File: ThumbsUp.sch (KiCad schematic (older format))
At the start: 159 parts, among them J17 Raiser_Female, J18 Raiser_Male, J19 52559-1233, J32 Battery, SW1 SW_Push, SW2 SW_DIP_x01, U1 ProMicro

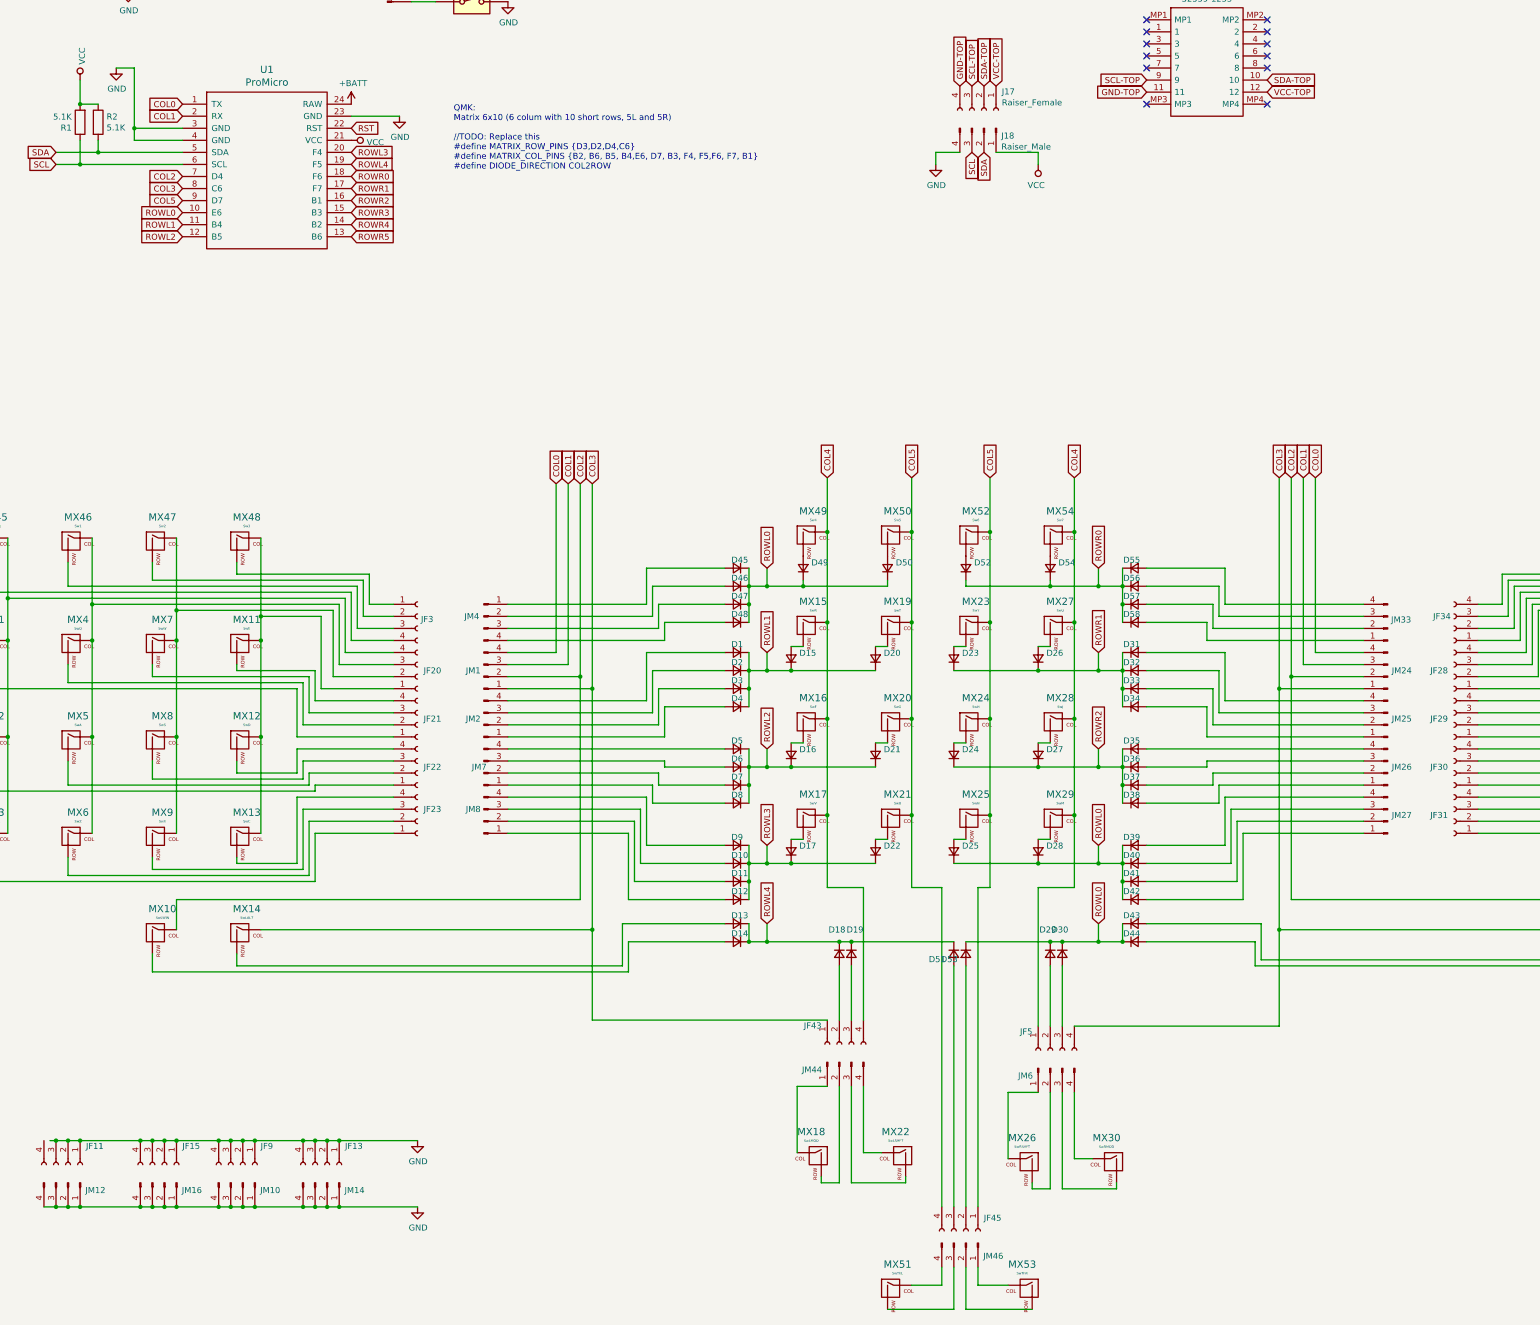
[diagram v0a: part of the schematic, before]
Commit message: Layed out switches and cross-plate connectors
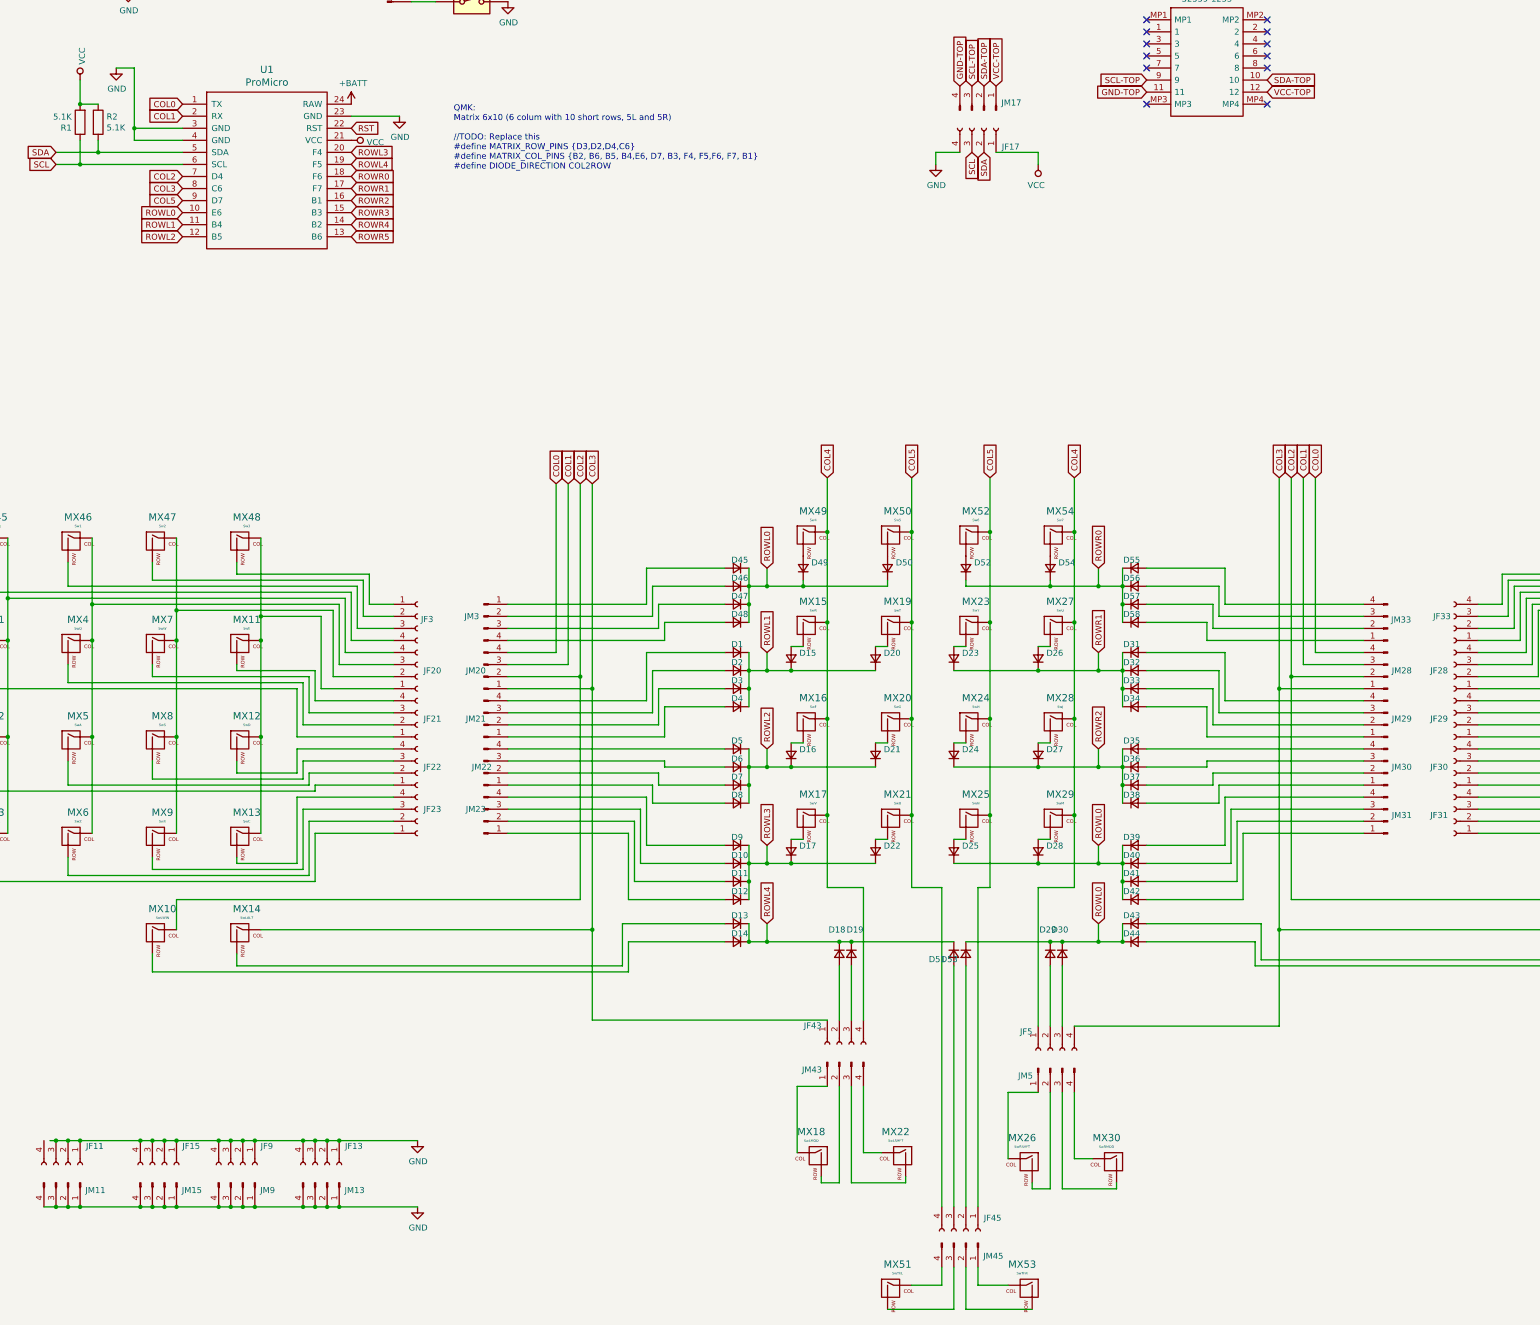
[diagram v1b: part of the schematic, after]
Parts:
- MX1, MX10, MX11, MX12, MX13, MX14, MX15, MX16, MX17, MX18, MX19, MX2, MX20, MX21, MX22, MX23, MX24, MX25, MX26, MX27, MX28, MX29, MX3, MX30, MX31, MX32, MX33, MX34, MX35, MX36, MX37, MX38, MX39, MX4, MX40, MX41, MX42, MX43, MX44, MX45, MX46, MX47, MX48, MX49, MX5, MX50, MX51, MX52, MX53, MX54, MX55, MX56, MX57, MX58, MX6, MX7, MX8, MX9: footprint keyswitches:Kailh_socket_PG1350_optional -> MX_Alps_Hybrid:MX-1U-NoLED_HotSwap
- renumbered J17 to JF17, JF34 to JF33, JM12 to JM11, JM14 to JM13, JM16 to JM15, J18 to JM17, JM1 to JM20, JM2 to JM21, JM7 to JM22, JM8 to JM23, JM24 to JM28, JM25 to JM29, JM4 to JM3, JM26 to JM30, JM27 to JM31, JM44 to JM43, JM46 to JM45, JM6 to JM5, JM10 to JM9
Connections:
- net GND: now also JF17.4 (Pin_4); no longer JM17.4 (Pin_4)
- net GND-TOP: now also JM17.4 (Pin_4); no longer JF17.4 (Pin_4)
- net SCL: now also JF17.3 (Pin_3); no longer JM17.3 (Pin_3)
- net SCL-TOP: now also JM17.3 (Pin_3); no longer JF17.3 (Pin_3)
- net SDA: now also JF17.2 (Pin_2); no longer JM17.2 (Pin_2)
- net SDA-TOP: now also JM17.2 (Pin_2); no longer JF17.2 (Pin_2)
- net VCC: now also JF17.1 (Pin_1); no longer JM17.1 (Pin_1)
- net VCC-TOP: now also JM17.1 (Pin_1); no longer JF17.1 (Pin_1)
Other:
- moved on the sheet: JF17, JM17

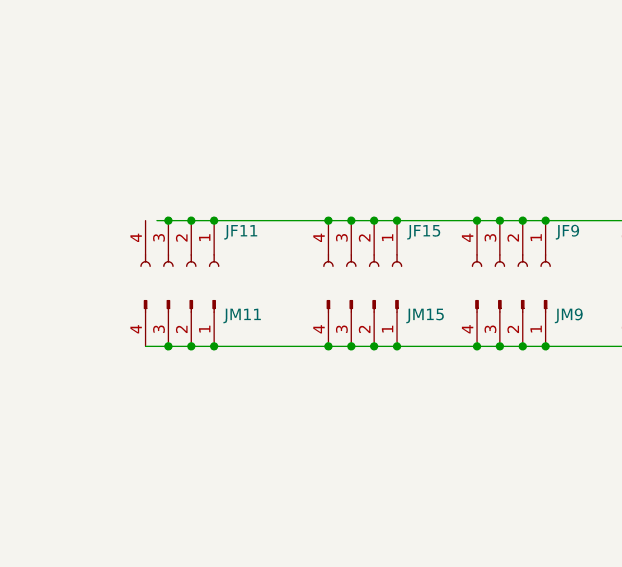
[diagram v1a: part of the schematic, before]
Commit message: Rotated the wings into 44 degree position, added the external boundary
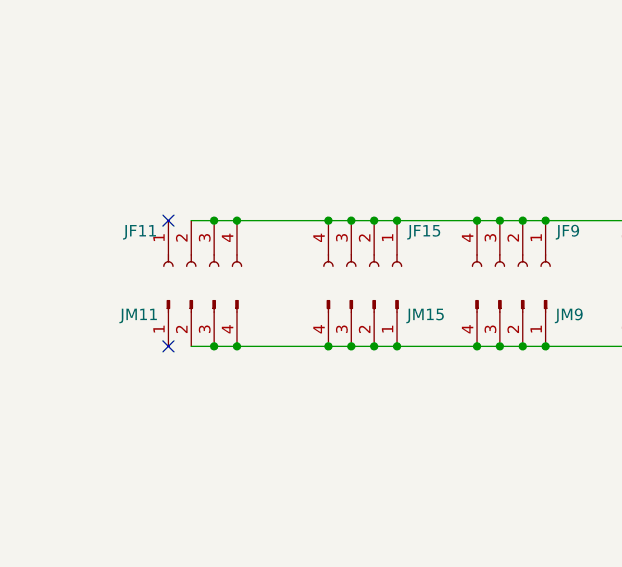
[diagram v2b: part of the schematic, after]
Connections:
- net GND: now also JF11.4 (Pin_4); no longer JF11.1 (Pin_1), JM11.1 (Pin_1)
- no-connect marks 13 -> 15
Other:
- moved on the sheet: JF11, JM11
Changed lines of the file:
@@
 F 3 "~" H 1950 11050 50  0001 C CNN
 	1    1950 11050
-	0    1    1    0
+	0    -1   1    0
 $EndComp
 $Comp
@@
 F 3 "~" H 1950 11200 50  0001 C CNN
 	1    1950 11200
-	0    1    1    0
+	0    -1   1    0
 $EndComp
 $Comp
@@
 	0    1    1    0
 $EndComp
-Wire Wire Line
-	1800 10850 1850 10850
-Connection ~ 1850 10850
-Wire Wire Line
-	1850 10850 1950 10850
-Connection ~ 1950 10850
-Wire Wire Line
-	1950 10850 2050 10850
-Connection ~ 2050 10850
-Wire Wire Line
-	2050 10850 2550 10850
 Connection ~ 2550 10850
 Wire Wire Line
@@
 Wire Wire Line
 	4200 10850 4850 10850
-Wire Wire Line
-	1750 11400 1850 11400
-Connection ~ 1850 11400
-Wire Wire Line
-	1850 11400 1950 11400
-Connection ~ 1950 11400
-Wire Wire Line
-	1950 11400 2050 11400
-Connection ~ 2050 11400
-Wire Wire Line
-	2050 11400 2550 11400
 Connection ~ 2550 11400
 Wire Wire Line
@@
 Wire Wire Line
 	9650 2650 10000 2650
+Wire Wire Line
+	2150 10850 2550 10850
+Wire Wire Line
+	1950 10850 2050 10850
+Connection ~ 2150 10850
+Connection ~ 2050 10850
+Wire Wire Line
+	2050 10850 2150 10850
+NoConn ~ 1850 10850
+Wire Wire Line
+	2150 11400 2550 11400
+Wire Wire Line
+	2150 11400 2050 11400
+Connection ~ 2150 11400
+Connection ~ 2050 11400
+Wire Wire Line
+	2050 11400 1950 11400
+NoConn ~ 1850 11400
 $EndSCHEMATC

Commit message: Routed L1 PCB
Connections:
- net COL0: now also JM20.1 (Pin_1), JM33.4 (Pin_4); no longer JM20.4 (Pin_4), JM28.4 (Pin_4)
- net COL1: now also JM20.2 (Pin_2), JM33.3 (Pin_3); no longer JM20.3 (Pin_3), JM28.3 (Pin_3)
- net COL2: now also JM20.3 (Pin_3), JM33.2 (Pin_2); no longer JM20.2 (Pin_2), JM28.2 (Pin_2)
- net COL3: now also JM20.4 (Pin_4), JM33.1 (Pin_1); no longer JM20.1 (Pin_1), JM28.1 (Pin_1)
- net GND: no longer JF11.2 (Pin_2), JF11.3 (Pin_3), JF11.4 (Pin_4), JF15.1 (Pin_1), JF15.2 (Pin_2), JF15.3 (Pin_3), JF15.4 (Pin_4), JF9.1 (Pin_1), JF9.2 (Pin_2), JF9.3 (Pin_3), JF9.4 (Pin_4), JM13.1 (Pin_1), JM13.2 (Pin_2), JM13.3 (Pin_3), JM13.4 (Pin_4)
- net at MX1.1 (COL), MX2.1 (COL), MX3.1 (COL)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: now also JF20.1 (Pin_1); no longer JF20.4 (Pin_4)
- net at MX1.2 (ROW): now also JF21.4 (Pin_4); no longer JF21.1 (Pin_1)
- net at MX4.1 (COL), MX46.1 (COL), MX5.1 (COL)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: now also JF20.2 (Pin_2); no longer JF20.3 (Pin_3)
- net at MX4.2 (ROW): now also JF21.3 (Pin_3); no longer JF21.2 (Pin_2)
- net at MX2.2 (ROW): now also JF22.4 (Pin_4); no longer JF22.1 (Pin_1)
- net at MX5.2 (ROW): now also JF22.3 (Pin_3); no longer JF22.2 (Pin_2)
- net at MX47.1 (COL), MX7.1 (COL), MX8.1 (COL)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: now also JF20.3 (Pin_3); no longer JF20.2 (Pin_2)
- net at MX7.2 (ROW): now also JF21.2 (Pin_2); no longer JF21.3 (Pin_3)
- net at MX11.1 (COL), MX12.1 (COL), MX13.1 (COL)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: now also JF20.4 (Pin_4); no longer JF20.1 (Pin_1)
- net at MX11.2 (ROW): now also JF21.1 (Pin_1); no longer JF21.4 (Pin_4)
- net at MX8.2 (ROW): now also JF22.2 (Pin_2); no longer JF22.3 (Pin_3)
- net at MX12.2 (ROW): now also JF22.1 (Pin_1); no longer JF22.4 (Pin_4)
- net at D5.2 (A): now also JM22.1 (Pin_1); no longer JM22.4 (Pin_4)
- net at D6.2 (A): now also JM22.2 (Pin_2); no longer JM22.3 (Pin_3)
- net at D7.2 (A): now also JM22.3 (Pin_3); no longer JM22.2 (Pin_2)
- net at D8.2 (A): now also JM22.4 (Pin_4); no longer JM22.1 (Pin_1)
- net at D1.2 (A): now also JM21.1 (Pin_1); no longer JM21.4 (Pin_4)
- net at D2.2 (A): now also JM21.2 (Pin_2); no longer JM21.3 (Pin_3)
- net at D3.2 (A): now also JM21.3 (Pin_3); no longer JM21.2 (Pin_2)
- net at D4.2 (A): now also JM21.4 (Pin_4); no longer JM21.1 (Pin_1)
- net at MX42.1 (COL), MX43.1 (COL), MX44.1 (COL)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: now also JF33.4 (Pin_4); no longer JF28.4 (Pin_4)
- net at MX42.2 (ROW): now also JF30.1 (Pin_1); no longer JF29.1 (Pin_1)
- net at MX39.1 (COL), MX40.1 (COL), MX41.1 (COL)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: now also JF33.3 (Pin_3); no longer JF28.3 (Pin_3)
- net at MX39.2 (ROW): now also JF30.2 (Pin_2); no longer JF29.2 (Pin_2)
- net at MX43.2 (ROW): now also JF29.1 (Pin_1); no longer JF30.1 (Pin_1)
- net at MX35.1 (COL), MX36.1 (COL), MX37.1 (COL)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: now also JF33.2 (Pin_2); no longer JF28.2 (Pin_2)
- net at MX35.2 (ROW): now also JF30.3 (Pin_3); no longer JF29.3 (Pin_3)
- net at MX31.1 (COL), MX32.1 (COL), MX33.1 (COL)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: now also JF33.1 (Pin_1); no longer JF28.1 (Pin_1)
- net at MX31.2 (ROW): now also JF30.4 (Pin_4); no longer JF29.4 (Pin_4)
- net at MX36.2 (ROW): now also JF29.3 (Pin_3); no longer JF30.3 (Pin_3)
- net at MX32.2 (ROW): now also JF29.4 (Pin_4); no longer JF30.4 (Pin_4)
- net at MX44.2 (ROW): now also JF28.1 (Pin_1); no longer JF31.1 (Pin_1)
- net at MX41.2 (ROW): now also JF28.2 (Pin_2); no longer JF31.2 (Pin_2)
- net at MX37.2 (ROW): now also JF28.3 (Pin_3); no longer JF31.3 (Pin_3)
- net at MX33.2 (ROW): now also JF28.4 (Pin_4); no longer JF31.4 (Pin_4)
- net at MX40.2 (ROW): now also JF29.2 (Pin_2); no longer JF30.2 (Pin_2)
- net at D35.2 (A): now also JM29.4 (Pin_4); no longer JM30.4 (Pin_4)
- net at D36.2 (A): now also JM29.3 (Pin_3); no longer JM30.3 (Pin_3)
- net at D37.2 (A): now also JM29.2 (Pin_2); no longer JM30.2 (Pin_2)
- net at D38.2 (A): now also JM29.1 (Pin_1); no longer JM30.1 (Pin_1)
- net at D31.2 (A): now also JM30.4 (Pin_4); no longer JM29.4 (Pin_4)
- net at D32.2 (A): now also JM30.3 (Pin_3); no longer JM29.3 (Pin_3)
- net at D33.2 (A): now also JM30.2 (Pin_2); no longer JM29.2 (Pin_2)
- net at D34.2 (A): now also JM30.1 (Pin_1); no longer JM29.1 (Pin_1)
- net at D39.2 (A): no longer JM31.4 (Pin_4)
- net at D40.2 (A): no longer JM31.3 (Pin_3)
- net at D41.2 (A): no longer JM31.2 (Pin_2)
- net at D42.2 (A): no longer JM31.1 (Pin_1)
- net at MX45.2 (ROW): now also JF3.1 (Pin_1); no longer JF3.4 (Pin_4)
- net at MX46.2 (ROW): now also JF3.2 (Pin_2); no longer JF3.3 (Pin_3)
- net at MX47.2 (ROW): now also JF3.3 (Pin_3); no longer JF3.2 (Pin_2)
- net at MX48.2 (ROW): now also JF3.4 (Pin_4); no longer JF3.1 (Pin_1)
- net at MX58.2 (ROW): now also JF31.1 (Pin_1); no longer JF33.1 (Pin_1)
- net at MX57.2 (ROW): now also JF31.2 (Pin_2); no longer JF33.2 (Pin_2)
- net at MX56.2 (ROW): now also JF31.3 (Pin_3); no longer JF33.3 (Pin_3)
- net at MX55.2 (ROW): now also JF31.4 (Pin_4); no longer JF33.4 (Pin_4)
- net at JM3.1 (Pin_1): now also D48.2 (A); no longer D45.2 (A)
- net at JM3.2 (Pin_2): now also D47.2 (A); no longer D46.2 (A)
- net at JM3.3 (Pin_3): now also D46.2 (A); no longer D47.2 (A)
- net at JM3.4 (Pin_4): now also D45.2 (A); no longer D48.2 (A)
- net at D58.2 (A): now also JM31.1 (Pin_1); no longer JM33.1 (Pin_1)
- net at D57.2 (A): now also JM31.2 (Pin_2); no longer JM33.2 (Pin_2)
- net at D56.2 (A): now also JM31.3 (Pin_3); no longer JM33.3 (Pin_3)
- net at D55.2 (A): now also JM31.4 (Pin_4); no longer JM33.4 (Pin_4)
- new net L1GND: JF11.2 (Pin_2), JF11.3 (Pin_3), JF11.4 (Pin_4), JF15.1 (Pin_1), JF15.2 (Pin_2), JF15.3 (Pin_3), JF15.4 (Pin_4), JF9.1 (Pin_1), JF9.2 (Pin_2), JF9.3 (Pin_3), JF9.4 (Pin_4)
- new net L3GND: JM13.1 (Pin_1), JM13.2 (Pin_2), JM13.3 (Pin_3), JM13.4 (Pin_4)
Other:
- moved on the sheet: JF13, JF28, JF29, JF30, JF31, JF33, JM13, JM28, JM29, JM30, JM31, JM33
